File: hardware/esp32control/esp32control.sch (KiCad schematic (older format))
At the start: 50 parts, among them J1 Conn_02x07_Odd_Even, P1 CONN_01X05, Q5 BSS138, Q6 BSS138, SW1 Boot, SW2 Reset, U1 ESP32-WROOM, U10 LTV-354T, U11 HUT4, U12 LM1117-3.3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

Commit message: pcb update
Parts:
- removed C1: 100n, Capacitors_SMD:C_0603, symbol esp32control-rescue:C_Small-device-esp32ValveControl-rescue
- removed J1: Conn_02x07_Odd_Even, Pin_Headers:Pin_Header_Straight_2x07_Pitch2.54mm, symbol Connector_Generic:Conn_02x07_Odd_Even
- removed P1: CONN_01X05, Pin_Headers:Pin_Header_Straight_1x05_Pitch2.54mm, symbol esp32control-rescue:CONN_01X05-conn-esp32ValveControl-rescue
- added J1: Conn_02x09_Odd_Even, Pin_Headers:Pin_Header_Straight_2x09_Pitch2.54mm, symbol Connector_Generic:Conn_02x09_Odd_Even
- added Q7, Q8: MMBT3904, Package_TO_SOT_SMD:SOT-23, symbol Transistor_BJT:MMBT3904
- added R20, R21: 10k, Resistors_SMD:R_0603, symbol esp32control-rescue:R-device-esp32ValveControl-rescue
- C23: value 100n -> 1u
- R3, R4, R5, R8: value 10k -> 1k5
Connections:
- net labels added: DTR, DTS, RTS, RXD0, TXD0
- wire segments 202 -> 214
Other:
- moved on the sheet: C23, R10, R11, SW2

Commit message: updated sch & pcb
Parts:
- removed J1: Conn_02x09_Odd_Even, Pin_Headers:Pin_Header_Straight_2x09_Pitch2.54mm, symbol Connector_Generic:Conn_02x09_Odd_Even
- added J1: Conn_02x10_Odd_Even, Pin_Headers:Pin_Header_Straight_2x10_Pitch2.54mm, symbol Connector_Generic:Conn_02x10_Odd_Even
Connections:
- wire segments 214 -> 216
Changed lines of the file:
@@
 Connection ~ 9400 1950
 Wire Wire Line
-	9600 3800 9600 4000
+	9600 3900 9600 4100
 $Comp
 L esp32control-rescue:GND-power-esp32ValveControl-rescue #PWR0107
 U 1 1 5C27C940
-P 9600 4000
-F 0 "#PWR0107" H 9600 3750 50  0001 C CNN
-F 1 "GND" H 9600 3850 50  0000 C CNN
-F 2 "" H 9600 4000 60  0000 C CNN
-F 3 "" H 9600 4000 60  0000 C CNN
-	1    9600 4000
+P 9600 4100
+F 0 "#PWR0107" H 9600 3850 50  0001 C CNN
+F 1 "GND" H 9600 3950 50  0000 C CNN
+F 2 "" H 9600 4100 60  0000 C CNN
+F 3 "" H 9600 4100 60  0000 C CNN
+	1    9600 4100
 	1    0    0    -1
 $EndComp
@@
 Wire Wire Line
 	9600 3600 10000 3600
-Wire Wire Line
-	9100 3700 8750 3700
-Wire Wire Line
-	9600 3700 10000 3700
 Text Label 9750 3400 0    60   ~ 0
 IO25
@@
 Text Label 6950 5150 0    60   ~ 0
 IO4
-Text Label 9750 3700 0    60   ~ 0
+Text Label 9750 3600 0    60   ~ 0
 SDA
-Text Label 8750 3700 0    60   ~ 0
+Text Label 8750 3600 0    60   ~ 0
 SCL
-Text Label 9750 3600 0    60   ~ 0
-IO5
-Text Label 8750 3600 0    60   ~ 0
-IO4
 $Comp
 L esp32control-rescue:GND-power-esp32ValveControl-rescue #PWR0108
 U 1 1 5C3B9271
-P 9100 4000
-F 0 "#PWR0108" H 9100 3750 50  0001 C CNN
-F 1 "GND" H 9100 3850 50  0000 C CNN
-F 2 "" H 9100 4000 60  0000 C CNN
-F 3 "" H 9100 4000 60  0000 C CNN
-	1    9100 4000
+P 9100 4100
+F 0 "#PWR0108" H 9100 3850 50  0001 C CNN
+F 1 "GND" H 9100 3950 50  0000 C CNN
+F 2 "" H 9100 4100 60  0000 C CNN
+F 3 "" H 9100 4100 60  0000 C CNN
+	1    9100 4100
 	1    0    0    -1
 $EndComp
 Wire Wire Line
-	9100 3800 9100 4000
+	9100 3900 9100 4100
 Wire Wire Line
 	6150 1300 6750 1300
@@
 Text Label 6950 5250 0    50   ~ 0
 nBoot
-$Comp
-L Connector_Generic:Conn_02x09_Odd_Even J1
-U 1 1 5CA34F1C
-P 9300 3400
-F 0 "J1" H 9350 4017 50  0000 C CNN
-F 1 "Conn_02x09_Odd_Even" H 9350 3926 50  0000 C CNN
-F 2 "Pin_Headers:Pin_Header_Straight_2x09_Pitch2.54mm" H 9300 3400 50  0001 C CNN
-F 3 "~" H 9300 3400 50  0001 C CNN
-	1    9300 3400
-	1    0    0    -1
-$EndComp
 Text Label 6950 4250 0    50   ~ 0
 TXD0
@@
 Text Label 8750 3200 0    50   ~ 0
 DTS
+$Comp
+L Connector_Generic:Conn_02x10_Odd_Even J1
+U 1 1 5CA6C5F1
+P 9300 3400
+F 0 "J1" H 9350 4017 50  0000 C CNN
+F 1 "Conn_02x10_Odd_Even" H 9350 3926 50  0000 C CNN
+F 2 "Pin_Headers:Pin_Header_Straight_2x10_Pitch2.54mm" H 9300 3400 50  0001 C CNN
+F 3 "~" H 9300 3400 50  0001 C CNN
+	1    9300 3400
+	1    0    0    -1
+$EndComp
+Wire Wire Line
+	9100 3700 8750 3700
+Wire Wire Line
+	9100 3800 8750 3800
+Wire Wire Line
+	9600 3700 10000 3700
+Wire Wire Line
+	9600 3800 10000 3800
+Text Label 8750 3700 0    50   ~ 0
+CH1
+Text Label 9750 3700 0    50   ~ 0
+CH2
+Text Label 8750 3800 0    50   ~ 0
+CH3
+Text Label 9750 3800 0    50   ~ 0
+CH4
 $EndSCHEMATC

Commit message: update libs to kicad 5.1.5
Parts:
- C2, C23, C26, C27, C4: footprint Capacitors_SMD:C_0603 -> Capacitor_SMD:C_0603_1608Metric
- C25, C28: footprint Capacitors_ThroughHole:C_Radial_D8_L11.5_P3.5 -> Capacitor_THT:CP_Radial_D8.0mm_P3.50mm
- C3: footprint Capacitors_SMD:C_0805_HandSoldering -> Capacitor_SMD:C_0805_2012Metric_Pad1.15x1.40mm_HandSolder
- D13, D4, D5, D6, D7: footprint Diodes_SMD:D_SMA -> Diode_SMD:D_SMA
- D14: footprint LEDs:LED_0603_HandSoldering -> LED_SMD:LED_0603_1608Metric_Pad1.05x0.95mm_HandSolder
- J1: footprint Pin_Headers:Pin_Header_Straight_2x10_Pitch2.54mm -> Connector_PinHeader_2.54mm:PinHeader_2x10_P2.54mm_Vertical
- L9: footprint smd_packages:WE-PD-7345 -> Inductor_SMD:L_7.3x7.3_H4.5
- R10, R11, R12, R13, R14, R15, R16, R17, R18, R19, R20, R21, R22, R23, R28, R29, R3, R30, R4, R5, R8, R9: footprint Resistors_SMD:R_0603 -> Resistor_SMD:R_0603_1608Metric; symbol esp32control-rescue:R-device-esp32ValveControl-rescue -> Device:R

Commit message: revB initial
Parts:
- removed C25: CP_Small, Capacitor_THT:CP_Radial_D8.0mm_P3.50mm, symbol esp32control-rescue:CP_Small-device-esp32ValveControl-rescue
- added BT1: Battery_Cell, Battery:BatteryHolder_Keystone_3001_1x12mm, symbol Device:Battery_Cell
- added C1: 1u, Capacitor_SMD:C_0603_1608Metric, symbol esp32control-rescue:C_Small-device-esp32ValveControl-rescue
- added C5, C6: 47u 10V, Capacitor_SMD:C_1206_3216Metric, symbol Device:C_Small
- added D15, D16: LED, LED_SMD:LED_0603_1608Metric_Pad1.05x0.95mm_HandSolder, symbol Device:LED
- added R31: 100, Resistor_SMD:R_0603_1608Metric, symbol Device:R
- added R32, R33: 1k, Resistor_SMD:R_0603_1608Metric, symbol Device:R
- added TP1: TestPoint, TestPoint:TestPoint_Pad_D1.5mm, symbol Connector:TestPoint
- added U13: RV-8523-C3, Package_SON:RTC_SMD_MicroCrystal_C3_2.5x3.7mm, symbol Timer_RTC:RV-8523-C3
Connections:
- net labels added: IO23
- net labels removed: DTS, IO5
- wire segments 216 -> 217
- no-connect marks 0 -> 13
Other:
- moved on the sheet: C23, D13, D14, D6, J1, Q5, Q6, Q7, Q8, R10, R11, R12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

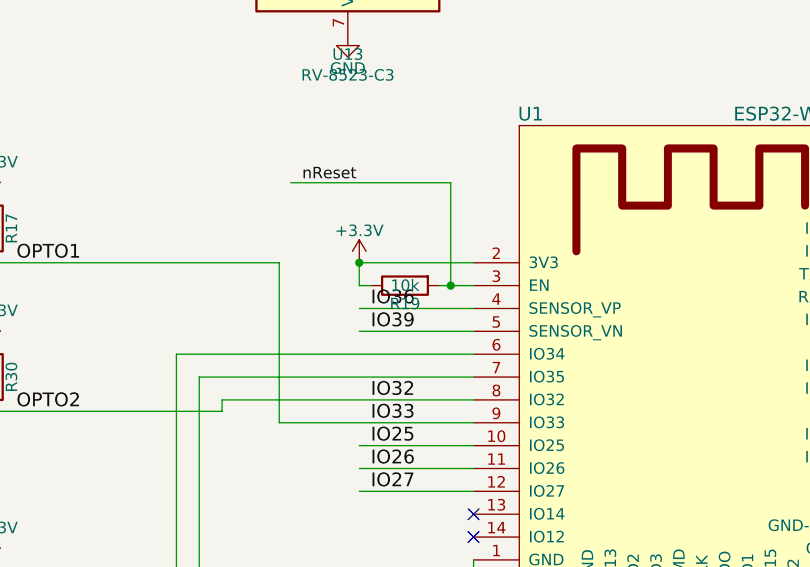
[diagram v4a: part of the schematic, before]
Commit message: switched position of con and esp in layout
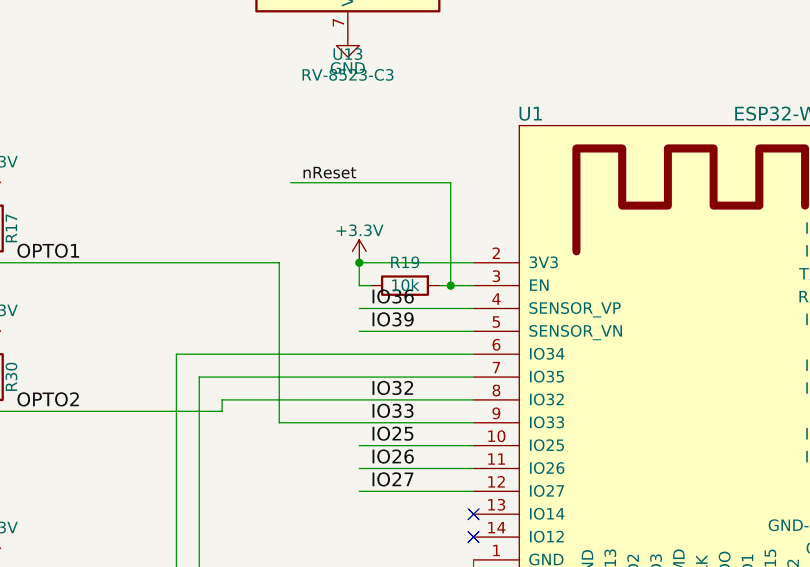
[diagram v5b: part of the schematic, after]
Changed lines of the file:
@@
 U 1 1 5B7F8F4F
 P 4150 4950
-F 0 "R19" V 4230 4950 50  0000 C CNN
+F 0 "R19" V 4050 4950 50  0000 C CNN
 F 1 "10k" V 4150 4950 50  0000 C CNN
 F 2 "Resistor_SMD:R_0603_1608Metric" V 4080 4950 30  0001 C CNN

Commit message: bom update
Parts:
- BT1: Mouser (none) -> 534-3001
- C28: value CP_Small -> 100u 50V; Mouser (none) -> 140-RGA101M1HBK0811G
- D13, D6: value D_Zener_Small -> SMAZ7V5; Mouser (none) -> 621-SMAZ7V5-F
- D4, D5: Mouser (none) -> 863-MBRS140T3G
- D7: value TVS -> SMAJ26CAQ; Mouser (none) -> 621-SMAJ26CAQ-13-F
- Q5, Q6: Mouser (none) -> 771-BSS138P215
- Q7, Q8: Mouser (none) -> 771-MMBT3904VL
- R14, R15: value tbd -> 100
- SW1, SW2: Mouser (none) -> 667-EVQ-Q2B03W
- U10, U5, U8, U9: Mouser (none) -> 859-LTV-354T
- U12: Mouser (none) -> 926-LM1117MP-3.3NOPB
- U13: Mouser (none) -> 428-201904-MG01
- U4: Mouser (none) -> 926-LM2675M-5.0/NOPB
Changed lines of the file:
@@
 F 2 "switches:SMD_Switch_6.5x6" H 7550 5900 60  0001 C CNN
 F 3 "" H 7550 5900 60  0000 C CNN
+F 4 " 667-EVQ-Q2B03W " H 7550 5900 50  0001 C CNN "Mouser"
 	1    7550 5900
 	1    0    0    -1
@@
 F 2 "Diode_SMD:D_SMA" H 10350 1550 60  0001 C CNN
 F 3 "" H 10350 1550 60  0000 C CNN
+F 4 " 863-MBRS140T3G " H 10350 1550 50  0001 C CNN "Mouser"
 	1    10350 1550
 	0    1    1    0
@@
 F 2 "Diode_SMD:D_SMA" H 8050 1000 60  0001 C CNN
 F 3 "" H 8050 1000 60  0000 C CNN
+F 4 " 863-MBRS140T3G " H 8050 1000 50  0001 C CNN "Mouser"
 	1    8050 1000
 	-1   0    0    1
@@
 P 8300 1100
 F 0 "C28" H 8300 1250 50  0000 L CNN
-F 1 "CP_Small" H 8150 950 50  0000 L CNN
+F 1 "100u 50V" H 8150 950 50  0000 L CNN
 F 2 "Capacitor_THT:CP_Radial_D8.0mm_P3.50mm" H 8300 1100 60  0001 C CNN
 F 3 "" H 8300 1100 60  0000 C CNN
+F 4 " 140-RGA101M1HBK0811G " H 8300 1100 50  0001 C CNN "Mouser"
 	1    8300 1100
 	1    0    0    -1
@@
 P 7850 1300
 F 0 "D7" H 7850 1450 50  0000 C CNN
-F 1 "TVS" H 7850 1150 50  0000 C CNN
+F 1 "SMAJ26CAQ" H 7850 1150 50  0000 C CNN
 F 2 "Diode_SMD:D_SMA" H 7850 1300 60  0001 C CNN
 F 3 "" H 7850 1300 60  0000 C CNN
+F 4 " 621-SMAJ26CAQ-13-F " H 7850 1300 50  0001 C CNN "Mouser"
 	1    7850 1300
 	0    1    1    0
@@
 F 2 "switches:SMD_Switch_6.5x6" H 7500 4850 60  0001 C CNN
 F 3 "" H 7500 4850 60  0000 C CNN
+F 4 " 667-EVQ-Q2B03W " H 7500 4850 50  0001 C CNN "Mouser"
 	1    7500 4850
 	1    0    0    -1
@@
 F 2 "SOIC_Packages:SO-4_4.4x3.6mm_Pitch2.54mm" H 1750 4750 50  0001 L CIN
 F 3 "http://optoelectronics.liteon.com/upload/download/DS70-2001-004/S_110_LTV-354T%2020140520.pdf" H 1975 4950 50  0001 L CNN
+F 4 " 859-LTV-354T " H 1950 4950 50  0001 C CNN "Mouser"
 	1    1950 4950
 	1    0    0    -1
@@
 F 2 "SOIC_Packages:SO-4_4.4x3.6mm_Pitch2.54mm" H 1750 5400 50  0001 L CIN
 F 3 "http://optoelectronics.liteon.com/upload/download/DS70-2001-004/S_110_LTV-354T%2020140520.pdf" H 1975 5600 50  0001 L CNN
+F 4 " 859-LTV-354T " H 1950 5600 50  0001 C CNN "Mouser"
 	1    1950 5600
 	1    0    0    -1
@@
 F 2 "SOIC_Packages:SO-4_4.4x3.6mm_Pitch2.54mm" H 1750 6350 50  0001 L CIN
 F 3 "http://optoelectronics.liteon.com/upload/download/DS70-2001-004/S_110_LTV-354T%2020140520.pdf" H 1975 6550 50  0001 L CNN
+F 4 " 859-LTV-354T " H 1950 6550 50  0001 C CNN "Mouser"
 	1    1950 6550
 	1    0    0    -1
@@
 F 2 "SOIC_Packages:SO-4_4.4x3.6mm_Pitch2.54mm" H 1750 7000 50  0001 L CIN
 F 3 "http://optoelectronics.liteon.com/upload/download/DS70-2001-004/S_110_LTV-354T%2020140520.pdf" H 1975 7200 50  0001 L CNN
+F 4 " 859-LTV-354T " H 1950 7200 50  0001 C CNN "Mouser"
 	1    1950 7200
 	1    0    0    -1
@@
 F 2 "Package_TO_SOT_SMD:SOT-23" H 8250 2875 50  0001 L CIN
 F 3 "https://www.fairchildsemi.com/datasheets/BS/BSS138.pdf" H 8050 2950 50  0001 L CNN
+F 4 " 771-BSS138P215 " H 8050 2950 50  0001 C CNN "Mouser"
 	1    8050 2950
 	0    1    1    0
@@
 F 2 "Package_TO_SOT_SMD:SOT-23" H 8500 3225 50  0001 L CIN
 F 3 "https://www.fairchildsemi.com/datasheets/BS/BSS138.pdf" H 8300 3300 50  0001 L CNN
+F 4 " 771-BSS138P215 " H 8300 3300 50  0001 C CNN "Mouser"
 	1    8300 3300
 	0    1    1    0
@@
 F 2 "SOIC_Packages:SOIC-8_3.9x4.9mm_Pitch1.27mm" H 9450 850 50  0001 L CIN
 F 3 "http://www.ti.com/lit/ds/symlink/lm2675.pdf" H 9400 1200 50  0001 C CNN
+F 4 " 926-LM2675M-5.0/NOPB " H 9400 1200 50  0001 C CNN "Mouser"
 	1    9400 1200
 	1    0    0    -1
@@
 F 2 "Package_TO_SOT_SMD:SOT-223-3_TabPin2" H 10450 2250 50  0001 C CNN
 F 3 "http://www.ti.com/lit/ds/symlink/lm1117.pdf" H 10450 2250 50  0001 C CNN
+F 4 " 926-LM1117MP-3.3NOPB " H 10450 2250 50  0001 C CNN "Mouser"
 	1    10450 2250
 	1    0    0    -1
@@
 U 1 1 5C2A8FC7
 P 4150 1900
-F 0 "R15" V 4230 1900 50  0000 C CNN
-F 1 "tbd" V 4150 1900 50  0000 C CNN
+F 0 "R15" V 4100 1700 50  0000 C CNN
+F 1 "100" V 4150 1900 50  0000 C CNN
 F 2 "Resistor_SMD:R_0603_1608Metric" V 4080 1900 30  0001 C CNN
 F 3 "" H 4150 1900 30  0000 C CNN
@@
 U 1 1 5C2A904F
 P 4150 1800
-F 0 "R14" V 4230 1800 50  0000 C CNN
-F 1 "tbd" V 4150 1800 50  0000 C CNN
+F 0 "R14" V 4100 1600 50  0000 C CNN
+F 1 "100" V 4150 1800 50  0000 C CNN
 F 2 "Resistor_SMD:R_0603_1608Metric" V 4080 1800 30  0001 C CNN
 F 3 "" H 4150 1800 30  0000 C CNN
@@
 P 8950 3550
 F 0 "D13" V 8904 3618 50  0000 L CNN
-F 1 "D_Zener_Small" V 8995 3618 50  0000 L CNN
+F 1 "SMAZ7V5" V 8995 3618 50  0000 L CNN
 F 2 "Diode_SMD:D_SMA" V 8950 3550 50  0001 C CNN
 F 3 "~" V 8950 3550 50  0001 C CNN
+F 4 " 621-SMAZ7V5-F " H 8950 3550 50  0001 C CNN "Mouser"
 	1    8950 3550
 	0    1    1    0
@@
 P 8750 3550
 F 0 "D6" V 8704 3618 50  0000 L CNN
-F 1 "D_Zener_Small" V 8795 3618 50  0000 L CNN
+F 1 "SMAZ7V5" V 8795 3618 50  0000 L CNN
 F 2 "Diode_SMD:D_SMA" V 8750 3550 50  0001 C CNN
 F 3 "~" V 8750 3550 50  0001 C CNN
+F 4 " 621-SMAZ7V5-F " H 8750 3550 50  0001 C CNN "Mouser"
 	1    8750 3550
 	0    1    1    0
@@
 F 2 "Package_TO_SOT_SMD:SOT-23" H 9350 5025 50  0001 L CIN
 F 3 "https://www.fairchildsemi.com/datasheets/2N/2N3904.pdf" H 9150 5100 50  0001 L CNN
+F 4 " 771-MMBT3904VL " H 9150 5100 50  0001 C CNN "Mouser"
 	1    9150 5100
 	-1   0    0    -1
@@
 F 2 "Package_TO_SOT_SMD:SOT-23" H 9350 5625 50  0001 L CIN
 F 3 "https://www.fairchildsemi.com/datasheets/2N/2N3904.pdf" H 9150 5700 50  0001 L CNN
+F 4 " 771-MMBT3904VL " H 9150 5700 50  0001 C CNN "Mouser"
 	1    9150 5700
 	-1   0    0    1
@@
 F 2 "Battery:BatteryHolder_Keystone_3001_1x12mm" V 3300 2910 50  0001 C CNN
 F 3 "~" V 3300 2910 50  0001 C CNN
+F 4 " 534-3001 " H 3300 2850 50  0001 C CNN "Mouser"
 	1    3300 2850
 	0    1    1    0
@@
 F 2 "Package_SON:RTC_SMD_MicroCrystal_C3_2.5x3.7mm" H 4900 3100 50  0001 C CNN
 F 3 "https://www.microcrystal.com/fileadmin/Media/Products/RTC/Datasheet/RV-8523-C3.pdf" H 3900 3450 50  0001 C CNN
+F 4 " 428-201904-MG01 " H 3900 3450 50  0001 C CNN "Mouser"
 	1    3900 3450
 	1    0    0    -1

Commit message: kicad6 update
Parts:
- C1, C23: value 1u -> 1u 10V; Mouser (none) -> 963-LMK107B7105KA-T
- C26, C27, C4: value 100n -> 100n 50V; Mouser (none) -> 80-C0603C104M5R
- C3: value 4u7 -> 4u7 16V; Mouser (none) -> 710-885012107013
- C5, C6: Mouser (none) -> 963-LMK316BC6476ML-T
- D14: value LED -> red; Mouser (none) -> 710-150060RS75000
- D15: value LED -> green; Mouser (none) -> 710-150060GS75000
- D16: value LED -> yellow; Mouser (none) -> 710-150060YS75000
- L9: value 680u -> 220u; Mouser (none) -> 710-74477728; Wuerth 74477728 -> (none)
- R19: value 10k -> nb
- U1: Mouser (none) -> 356-ESP32WRM32UE28UH
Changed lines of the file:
@@
 P 7750 6050
 F 0 "C23" H 7760 6120 50  0000 L CNN
-F 1 "1u" H 7760 5970 50  0000 L CNN
+F 1 "1u 10V" H 7760 5970 50  0000 L CNN
 F 2 "Capacitor_SMD:C_0603_1608Metric" H 7750 6050 60  0001 C CNN
 F 3 "" H 7750 6050 60  0000 C CNN
+F 4 " 963-LMK107B7105KA-T " H 7750 6050 50  0001 C CNN "Mouser"
 	1    7750 6050
 	-1   0    0    -1
@@
 P 10500 1400
 F 0 "L9" H 10530 1440 50  0000 L CNN
-F 1 "680u" H 10530 1360 50  0000 L CNN
+F 1 "220u" H 10530 1360 50  0000 L CNN
 F 2 "Inductor_SMD:L_7.3x7.3_H4.5" H 10500 1400 60  0001 C CNN
 F 3 "" H 10500 1400 60  0000 C CNN
-F 4 "74477728" H 10500 1400 60  0001 C CNN "Wuerth"
+F 4 "" H 10500 1400 60  0001 C CNN "Wuerth"
+F 5 " 710-74477728 " H 10500 1400 50  0001 C CNN "Mouser"
 	1    10500 1400
 	0    -1   -1   0
@@
 P 8650 1100
 F 0 "C27" H 8660 1170 50  0000 L CNN
-F 1 "100n" H 8660 1020 50  0000 L CNN
+F 1 "100n 50V" H 8660 1020 50  0000 L CNN
 F 2 "Capacitor_SMD:C_0603_1608Metric" H 8650 1100 60  0001 C CNN
 F 3 "" H 8650 1100 60  0000 C CNN
+F 4 " 80-C0603C104M5R " H 8650 1100 50  0001 C CNN "Mouser"
 	1    8650 1100
 	1    0    0    -1
@@
 P 10600 1500
 F 0 "C26" H 10610 1570 50  0000 L CNN
-F 1 "100n" H 10610 1420 50  0000 L CNN
+F 1 "100n 50V" H 10610 1420 50  0000 L CNN
 F 2 "Capacitor_SMD:C_0603_1608Metric" H 10600 1500 60  0001 C CNN
 F 3 "" H 10600 1500 60  0000 C CNN
+F 4 " 80-C0603C104M5R " H 10600 1500 50  0001 C CNN "Mouser"
 	1    10600 1500
 	1    0    0    -1
@@
 F 2 "ESP32-footprints-Lib:ESP32-WROOM" H 5750 6800 60  0001 C CNN
 F 3 "" H 4950 5900 60  0001 C CNN
+F 4 " 356-ESP32WRM32UE28UH " H 5400 5450 50  0001 C CNN "Mouser"
 	1    5400 5450
 	1    0    0    -1
@@
 P 4150 4950
 F 0 "R19" V 4050 4950 50  0000 C CNN
-F 1 "10k" V 4150 4950 50  0000 C CNN
+F 1 "nb" V 4150 4950 50  0000 C CNN
 F 2 "Resistor_SMD:R_0603_1608Metric" V 4080 4950 30  0001 C CNN
 F 3 "" H 4150 4950 30  0000 C CNN
@@
 P 11000 2350
 F 0 "C4" H 11010 2420 50  0000 L CNN
-F 1 "100n" H 11010 2270 50  0000 L CNN
+F 1 "100n 50V" H 11010 2270 50  0000 L CNN
 F 2 "Capacitor_SMD:C_0603_1608Metric" H 11000 2350 60  0001 C CNN
 F 3 "" H 11000 2350 60  0000 C CNN
+F 4 " 80-C0603C104M5R " H 11000 2350 50  0001 C CNN "Mouser"
 	1    11000 2350
 	1    0    0    -1
@@
 P 10800 2350
 F 0 "C3" H 10810 2420 50  0000 L CNN
-F 1 "4u7" H 10810 2270 50  0000 L CNN
+F 1 "4u7 16V" H 10810 2270 50  0000 L CNN
 F 2 "Capacitor_SMD:C_0805_2012Metric_Pad1.15x1.40mm_HandSolder" H 10800 2350 60  0001 C CNN
 F 3 "" H 10800 2350 60  0000 C CNN
+F 4 " 710-885012107013 " H 10800 2350 50  0001 C CNN "Mouser"
 	1    10800 2350
 	1    0    0    -1
@@
 P 9900 2100
 F 0 "D14" V 9938 1983 50  0000 R CNN
-F 1 "LED" V 9847 1983 50  0000 R CNN
+F 1 "red" V 9847 1983 50  0000 R CNN
 F 2 "LED_SMD:LED_0603_1608Metric_Pad1.05x0.95mm_HandSolder" H 9900 2100 50  0001 C CNN
 F 3 "~" H 9900 2100 50  0001 C CNN
+F 4 " 710-150060RS75000 " H 9900 2100 50  0001 C CNN "Mouser"
 	1    9900 2100
 	0    -1   -1   0
@@
 P 3700 3000
 F 0 "C1" H 3710 3070 50  0000 L CNN
-F 1 "1u" H 3710 2920 50  0000 L CNN
+F 1 "1u 10V" H 3710 2920 50  0000 L CNN
 F 2 "Capacitor_SMD:C_0603_1608Metric" H 3700 3000 60  0001 C CNN
 F 3 "" H 3700 3000 60  0000 C CNN
+F 4 " 963-LMK107B7105KA-T " H 3700 3000 50  0001 C CNN "Mouser"
 	1    3700 3000
 	0    1    -1   0
@@
 P 5150 950
 F 0 "D15" V 5188 833 50  0000 R CNN
-F 1 "LED" V 5097 833 50  0000 R CNN
+F 1 "green" V 5097 833 50  0000 R CNN
 F 2 "LED_SMD:LED_0603_1608Metric_Pad1.05x0.95mm_HandSolder" H 5150 950 50  0001 C CNN
 F 3 "~" H 5150 950 50  0001 C CNN
+F 4 " 710-150060GS75000 " H 5150 950 50  0001 C CNN "Mouser"
 	1    5150 950
 	0    -1   -1   0
@@
 P 7150 950
 F 0 "D16" V 7188 833 50  0000 R CNN
-F 1 "LED" V 7097 833 50  0000 R CNN
+F 1 "yellow" V 7097 833 50  0000 R CNN
 F 2 "LED_SMD:LED_0603_1608Metric_Pad1.05x0.95mm_HandSolder" H 7150 950 50  0001 C CNN
 F 3 "~" H 7150 950 50  0001 C CNN
+F 4 " 710-150060YS75000 " H 7150 950 50  0001 C CNN "Mouser"
 	1    7150 950
 	0    -1   -1   0
@@
 F 2 "Capacitor_SMD:C_1206_3216Metric" H 10800 1500 50  0001 C CNN
 F 3 "~" H 10800 1500 50  0001 C CNN
+F 4 " 963-LMK316BC6476ML-T " H 10800 1500 50  0001 C CNN "Mouser"
 	1    10800 1500
 	1    0    0    -1
@@
 F 2 "Capacitor_SMD:C_1206_3216Metric" H 11050 1500 50  0001 C CNN
 F 3 "~" H 11050 1500 50  0001 C CNN
+F 4 " 963-LMK316BC6476ML-T " H 11050 1500 50  0001 C CNN "Mouser"
 	1    11050 1500
 	1    0    0    -1
